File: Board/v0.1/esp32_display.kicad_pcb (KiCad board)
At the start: 2 copper layers, 90.5 x 69 mm, 53 parts, among them J1 USB_B_Micro, J2 Conn_01x06_Male, SW1 RST_BTN, SW2 SCREEN_OFF_BTN, U1 ESP32-WROOM-32, U2 MAX1821, U3 Display_ILI9341

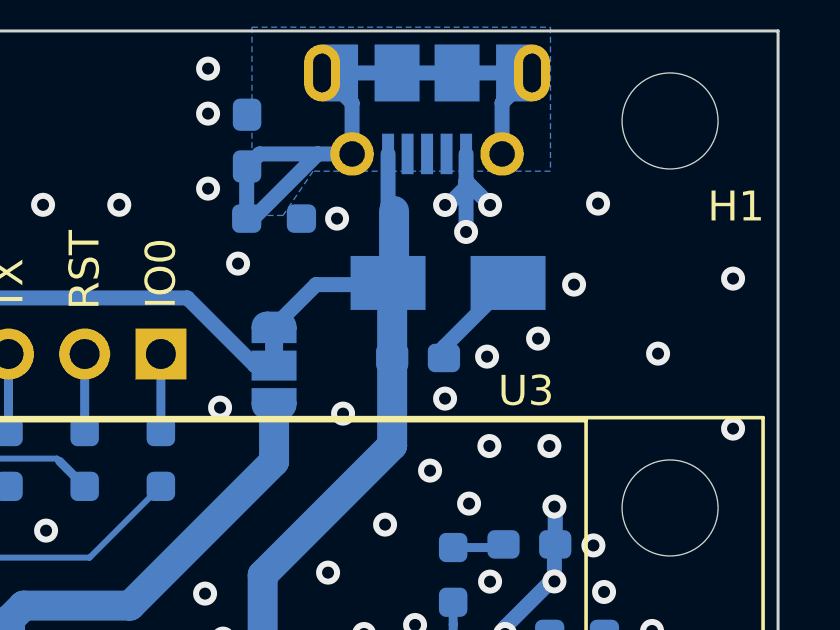
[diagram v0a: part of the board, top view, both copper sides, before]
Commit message: Clean schematics (add date and revision...)
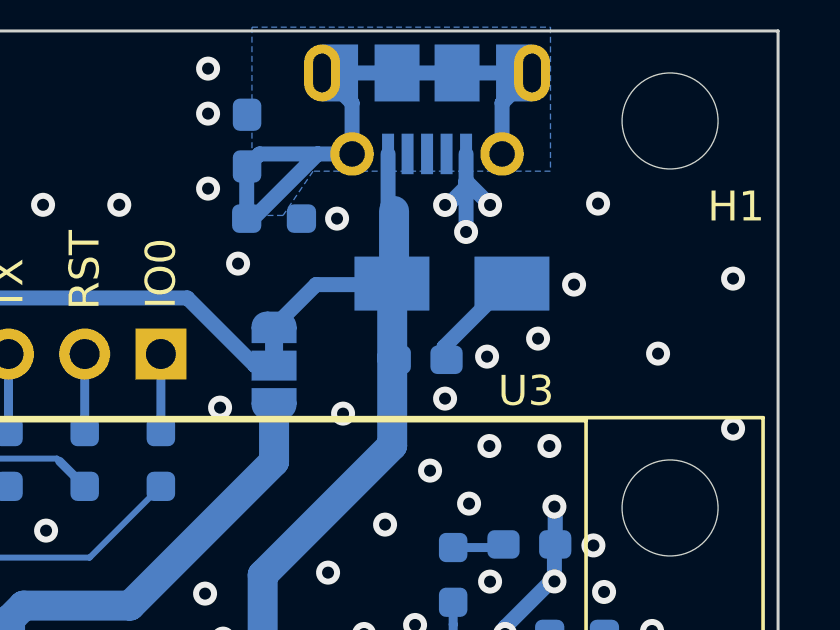
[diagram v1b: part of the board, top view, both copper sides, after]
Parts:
- moved D1 0.13 mm to (166.6, 40.4)
- moved C2 0.11 mm to (165.6, 43.0)

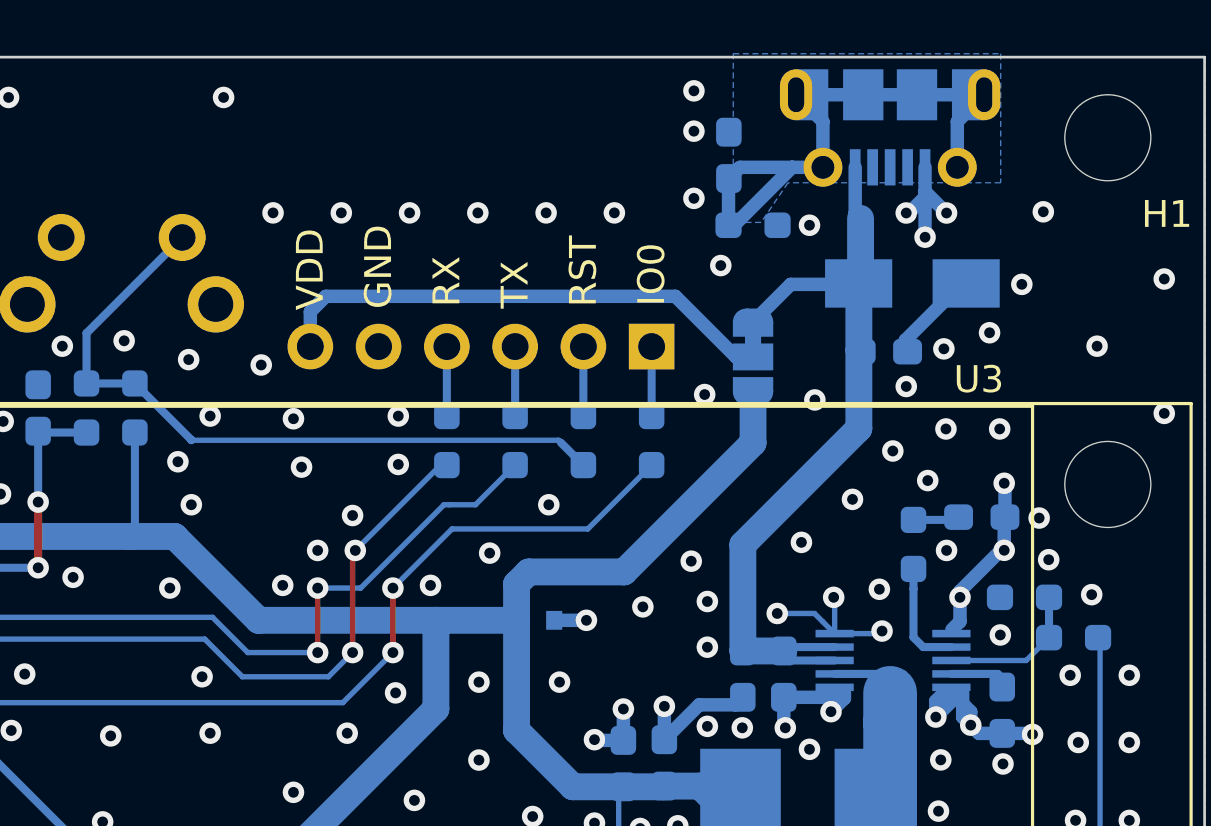
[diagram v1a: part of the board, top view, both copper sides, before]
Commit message: Add polyfuse, 3.3V status LED, USB_CONN sheet
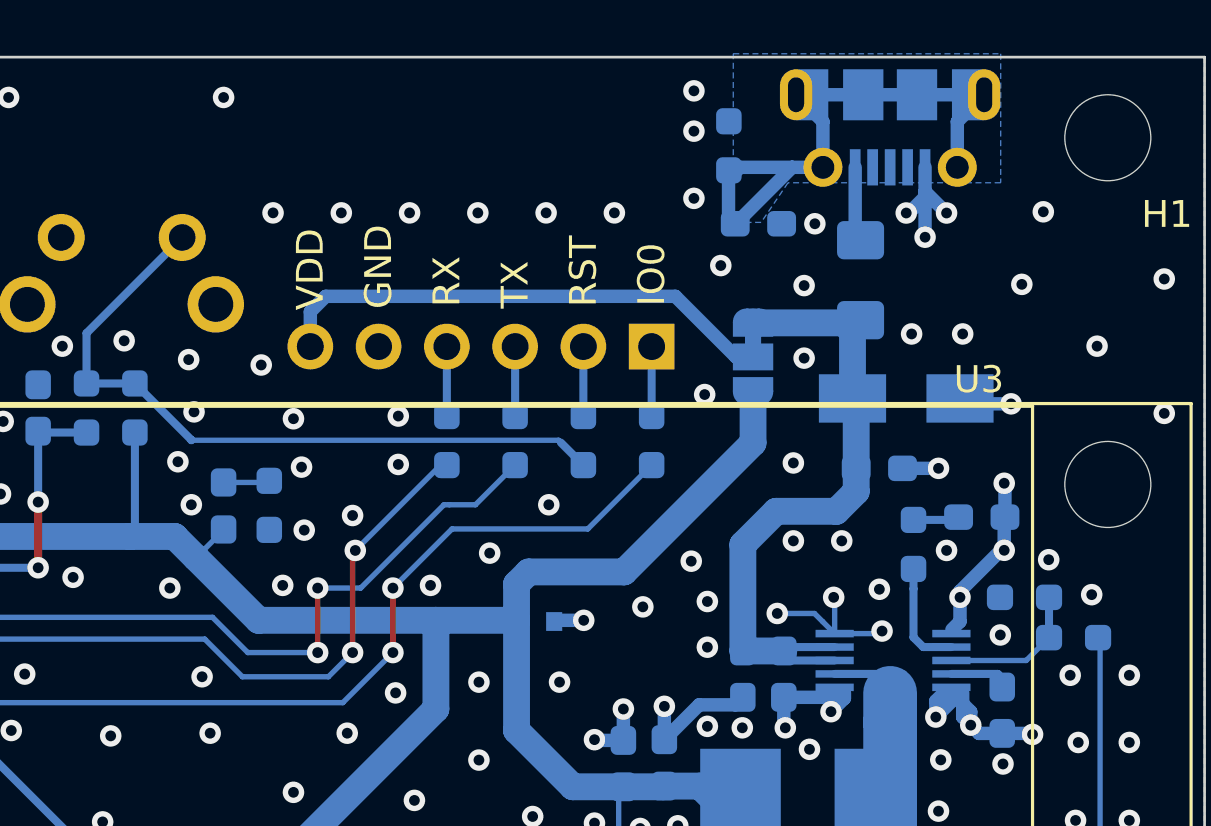
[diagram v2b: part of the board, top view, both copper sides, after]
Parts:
- removed the C1 at (159.8, 35.7)
- removed the C2 at (165.6, 43.0)
- removed the D1 at (166.6, 40.4)
- removed the J1 at (165.8, 34.6)
- removed the R1 at (160.7, 38.3)
- added C14: 4.7nF, Capacitor_SMD:C_0603_1608Metric_Pad1.08x0.95mm_HandSolder, B.Cu at (160.9, 38.2)
- added C15: 4.7uF, Capacitor_SMD:C_0603_1608Metric_Pad1.08x0.95mm_HandSolder, B.Cu at (165.4, 47.3)
- added D3: GREEN_LED, Diode_SMD:D_0603_1608Metric_Pad1.05x0.95mm_HandSolder, B.Cu at (141.0, 48.7)
- added D4: SMAJ5.0CA, Diode_SMD:D_SMA, B.Cu at (166.4, 44.7)
- added F1: 500mA, 1A, Fuse:Fuse_1206_3216Metric_Pad1.42x1.75mm_HandSolder, B.Cu at (164.7, 40.3)
- added J2: USB_B_Micro, myLib:USB_Micro-B_Molex-105017-0001, B.Cu at (165.8, 34.6)
- added R20: 1.5k, Resistor_SMD:R_0603_1608Metric_Pad0.98x0.95mm_HandSolder, B.Cu at (142.7, 48.7)
- added R24: 1M, Resistor_SMD:R_0603_1608Metric_Pad0.98x0.95mm_HandSolder, B.Cu at (159.8, 35.3)
- D1: renamed from D3; value LED -> RED_LED
- renumbered C3 to C1, C12 to C10, C13 to C11, C14 to C12, C15 to C13, C4 to C2, C5 to C3, C6 to C4, C7 to C5, C8 to C6, C9 to C7, C10 to C8, C11 to C9, J2 to J1, R2 to R1, R11 to R10, R12 to R11, R13 to R12, R14 to R13, R15 to R14, R16 to R15, R17 to R16, R18 to R17, R19 to R18, R20 to R19, R3 to R2, R4 to R3, R5 to R4, R6 to R5, R7 to R6, R8 to R7, R9 to R8, R10 to R9
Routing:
- net Net-(C14-Pad1): track 0.00 -> 21.9 mm
- net Net-(C1-Pad1): track 21.9 -> 0.00 mm
- net +5V: track 29.9 -> 24.7 mm
- net Net-(F1-Pad2): track 0.00 -> 2.81 mm
- net Net-(D3-Pad1): track 0.00 -> 1.72 mm
- net +3V3: track 224.8 -> 226.3 mm
- net GND: track 74.3 -> 74.1 mm, vias 367 -> 365
- added copper zone on B.Cu, net (none)
- removed copper zone on B.Cu, net Net-(C1-Pad1)
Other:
- board text added: "3.3V PWR"
- board text added: "5V - 1, 2 3.3V - 2, 3"
- board text added: "JP1-VDD sel"
- board text removed: "5V"

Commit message: Fix missing pad for H1, fix missing power input ERC error
ERC error was: Input power pin not driven by any output power pins.
Fix was adding PWR_FLAG power symbol after polyfuse or inductor.
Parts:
- H1: value MountingHole_Pad -> MountingHole
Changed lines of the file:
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@@
     (property "Sheetname" "")
     (attr exclude_from_pos_files)
-    (fp_text reference "H1" (at 2.2 2.855) (layer "F.SilkS")
+    (fp_text reference "H1" (at 0 3.7) (layer "F.SilkS")
       (effects (font (size 1 1) (thickness 0.15)))
     )
-    (fp_text value "MountingHole_Pad" (at 0 3.75) (layer "F.Fab")
+    (fp_text value "MountingHole" (at 0 3.75) (layer "F.Fab")
       (effects (font (size 1 1) (thickness 0.15)))
     )
@@
     (fp_circle (center 0 0) (end 2.75 0) (layer "Cmts.User") (width 0.15) (fill none))
     (fp_circle (center 0 0) (end 3 0) (layer "F.CrtYd") (width 0.05) (fill none))
-    (pad "" np_thru_hole circle (at 0 0) (size 3.2 3.2) (drill 3.2) (layers F&B.Cu *.Mask))
+    (pad "" np_thru_hole circle locked (at 0 0) (size 3.2 3.2) (drill 3.2) (layers *.Cu *.Mask))
   )
   (footprint "Capacitor_SMD:C_0603_1608Metric_Pad1.08x0.95mm_HandSolder" (layer "B.Cu")

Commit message: Add KiBot DRC filters
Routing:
- added copper zone on B.Cu, net Net-(C14-Pad1)
- removed copper zone on B.Cu, net (none)
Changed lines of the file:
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@@
     )
   )
-  (zone (net 0) (net_name "") (layer "B.Cu") (hatch edge 0.508)
+  (zone (net 9) (net_name "Net-(C14-Pad1)") (layer "B.Cu") (hatch edge 0.508)
     (priority 2)
     (connect_pads (clearance 0.254))

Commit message: Generate gerbers, sch and BOM with KiBot
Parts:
- added REF**: FCC-Logo_7.3x6mm_SilkScreen, Symbol:FCC-Logo_7.3x6mm_SilkScreen, B.Cu at (151.8, 94.2)
- added REF**: OSHW-Logo_7.5x8mm_SilkScreen, Symbol:OSHW-Logo_7.5x8mm_SilkScreen, B.Cu at (113.4, 81.7)
- added REF**: CE-Logo_8.5x6mm_SilkScreen, Symbol:CE-Logo_8.5x6mm_SilkScreen, B.Cu at (140.8, 94.2)

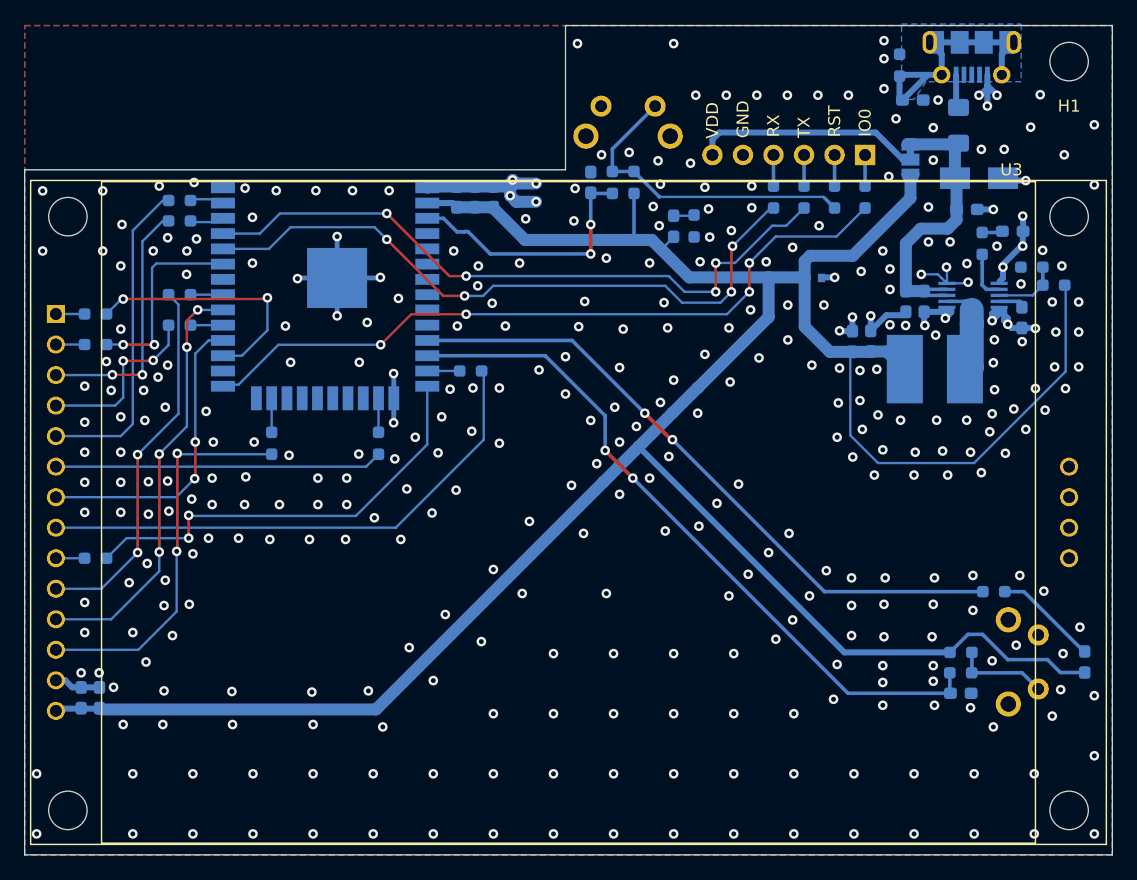
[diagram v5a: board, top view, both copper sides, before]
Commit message: Fix some via position, chane Net-(J1-Pad6) trace width
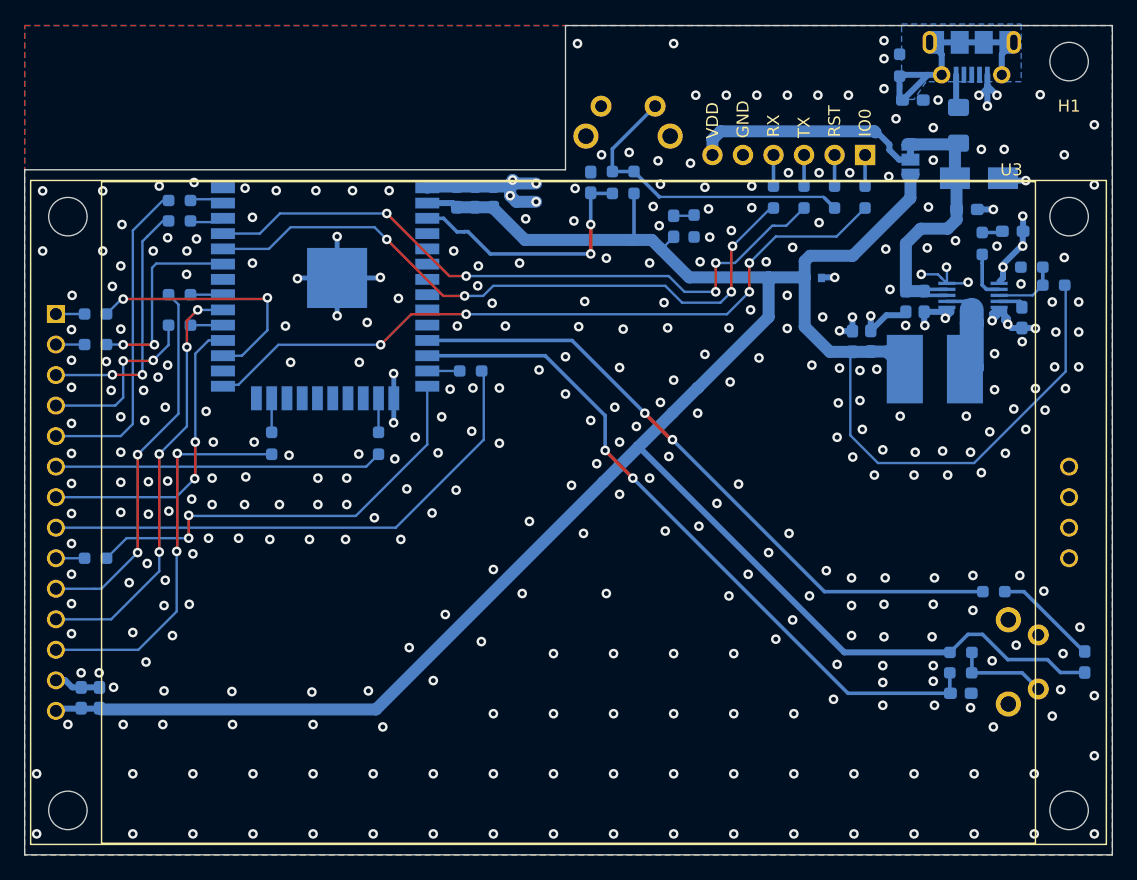
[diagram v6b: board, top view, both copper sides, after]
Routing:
- net GND: vias 365 -> 364
